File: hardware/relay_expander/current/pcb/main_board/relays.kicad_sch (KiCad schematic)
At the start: 82 parts, among them J10 Screw_Terminal_01x02, J11 Screw_Terminal_01x02, J4 Screw_Terminal_01x02, J5 Screw_Terminal_01x02, J6 Screw_Terminal_01x02, J7 Screw_Terminal_01x02, J8 Screw_Terminal_01x02, J9 Screw_Terminal_01x02, K1 SANYOU_SRD_Form_C, K2 SANYOU_SRD_Form_C, K3 SANYOU_SRD_Form_C, K4 SANYOU_SRD_Form_C, K5 SANYOU_SRD_Form_C, K6 SANYOU_SRD_Form_C, K7 SANYOU_SRD_Form_C, K8 SANYOU_SRD_Form_C, Q1 BC548, Q2 BC548, Q3 BC548, Q4 BC548, Q5 BC548, Q6 BC548, Q7 BC548, Q8 BC548, U2 TCMT4100, U3 TCMT4100

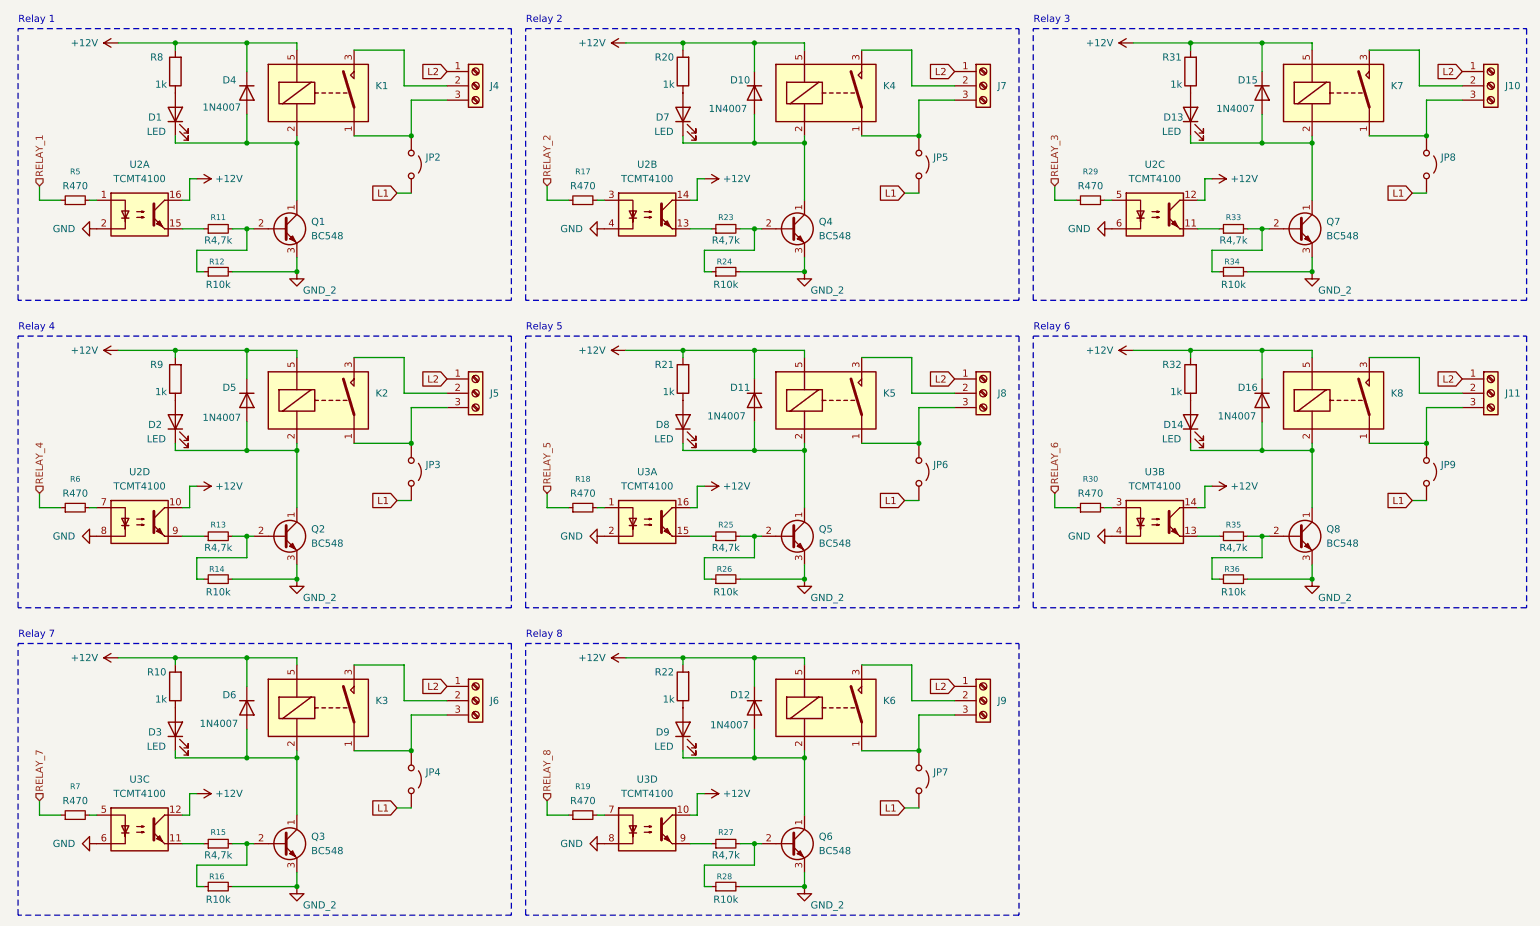
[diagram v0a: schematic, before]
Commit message: [ADD] ui board template
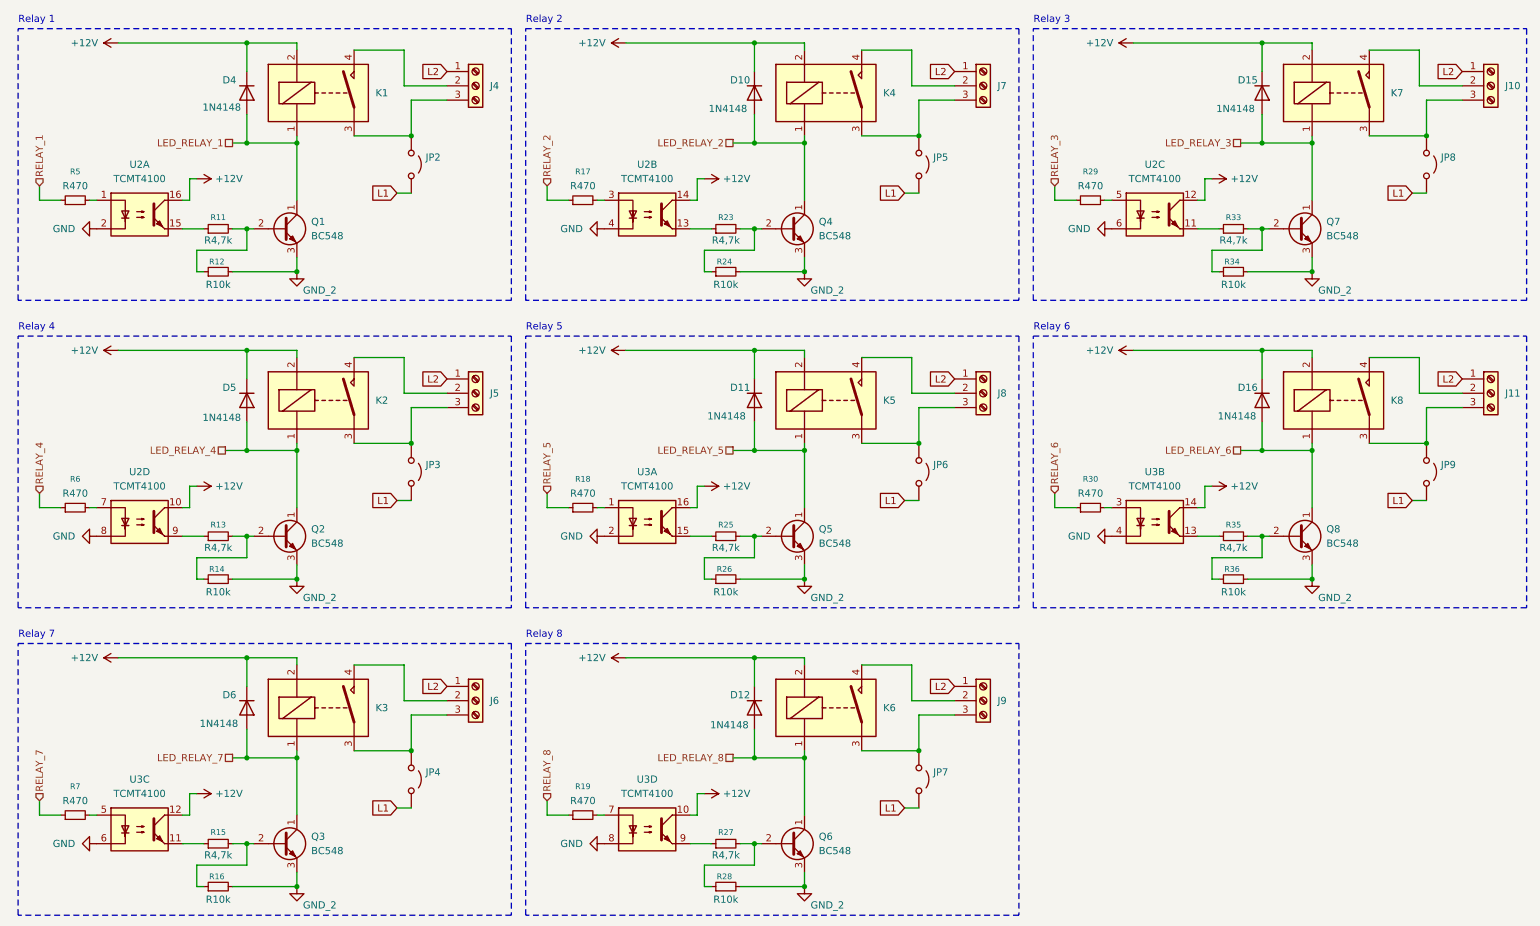
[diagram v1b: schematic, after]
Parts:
- removed D1, D13, D14, D2, D3, D7, D8, D9: LED, LED_SMD:LED_1206_3216Metric_Pad1.42x1.75mm_HandSolder, symbol Device:LED
- removed R10, R20, R21, R22, R31, R32, R8, R9: 1k, Resistor_SMD:R_1206_3216Metric_Pad1.30x1.75mm_HandSolder, symbol Device:R
- D10, D11, D12, D15, D16, D4, D5, D6: value 1N4007 -> 1N4148; footprint (none) -> Diode_SMD:D_SOD-123
- J10, J11, J5, J6, J7, J9: footprint Project_Parts_Footprints_Lib:TerminalBlock_Phoenix_MPT-0,5-3-2.54_1x03_P2.54mm_Horizontal -> footprints:Terminal_block_1x3_2,54
- J4: footprint Project_Parts_Footprints_Lib:TerminalBlock_Phoenix_MPT-0,5-3-2.54_1x03_P2.54mm_Horizontal -> TerminalBlock:TerminalBlock_Xinya_XY308-2.54-3P_1x03_P2.54mm_Horizontal
- J8: value Screw_Terminal_01x02 -> Screw_Terminal_01x03; footprint Project_Parts_Footprints_Lib:TerminalBlock_Phoenix_MPT-0,5-3-2.54_1x03_P2.54mm_Horizontal -> footprints:Terminal_block_1x3_2,54
- K1, K2, K3, K4, K5, K6, K7, K8: value SANYOU_SRD_Form_C -> HF46F-12-HS1; footprint templates_lib_footprints:Songle_SMI-SL-A -> homeautomation_core:relay_HF46F; symbol Relay:SANYOU_SRD_Form_A -> homeautomation_core:Relay_HF46F_Form_A
- R11, R12, R13, R14, R15, R16, R17, R18, R19, R23, R24, R25, R26, R27, R28, R29, R30, R33, R34, R35, R36, R5, R6, R7: footprint (none) -> Resistor_SMD:R_1206_3216Metric_Pad1.30x1.75mm_HandSolder
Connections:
- net +12V: now also K1.2, K2.2, K3.2, K4.2, K5.2, K6.2, K7.2, K8.2; no longer K1.5, K2.5, K3.5, K4.5, K5.5, K6.5, K7.5, K8.5
- net at J5.3 (Pin_3), JP3.1 (A): now also K2.3; no longer K2.1
- net LED_RELAY_6: now reaches D16.2 (A), Q8.1 (C)
- net LED_RELAY_6: now also K8.1; no longer K8.2
- net LED_RELAY_8: now reaches D12.2 (A), Q6.1 (C)
- net LED_RELAY_8: now also K6.1; no longer K6.2
- net LED_RELAY_4: now reaches D5.2 (A), Q2.1 (C)
- net LED_RELAY_4: now also K2.1; no longer K2.2
- net at J5.2 (Pin_2): now also K2.4; no longer K2.3
- net at J7.2 (Pin_2): now also K4.4; no longer K4.3
- net at J7.3 (Pin_3), JP5.1 (A): now also K4.3; no longer K4.1
- net at J11.3 (Pin_3), JP9.1 (A): now also K8.3; no longer K8.1
- net at J8.2 (Pin_2): now also K5.4; no longer K5.3
- net at J8.3 (Pin_3), JP6.1 (A): now also K5.3; no longer K5.1
- net LED_RELAY_5: now reaches D11.2 (A), Q5.1 (C)
- net LED_RELAY_5: now also K5.1; no longer K5.2
- net LED_RELAY_1: now reaches D4.2 (A), Q1.1 (C)
- net LED_RELAY_1: now also K1.1; no longer K1.2
- net LED_RELAY_7: now reaches D6.2 (A), Q3.1 (C)
- net LED_RELAY_7: now also K3.1; no longer K3.2
- net at J6.3 (Pin_3), JP4.1 (A): now also K3.3; no longer K3.1
- net at J6.2 (Pin_2): now also K3.4; no longer K3.3
- net at J10.2 (Pin_2): now also K7.4; no longer K7.3
- net at J10.3 (Pin_3), JP8.1 (A): now also K7.3; no longer K7.1
- net at J11.2 (Pin_2): now also K8.4; no longer K8.3
- net LED_RELAY_3: now reaches D15.2 (A), Q7.1 (C)
- net LED_RELAY_3: now also K7.1; no longer K7.2
- net LED_RELAY_2: now reaches D10.2 (A), Q4.1 (C)
- net LED_RELAY_2: now also K4.1; no longer K4.2
- net at J9.3 (Pin_3), JP7.1 (A): now also K6.3; no longer K6.1
- net at J9.2 (Pin_2): now also K6.4; no longer K6.3
- net at J4.2 (Pin_2): now also K1.4; no longer K1.3
- net at J4.3 (Pin_3), JP2.1 (A): now also K1.3; no longer K1.1

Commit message: [ADD] board connector
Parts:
- renumbered K4 to K2, K7 to K3, K2 to K4, K8 to K6, K3 to K7, K6 to K8, Q4 to Q2, Q7 to Q3, Q2 to Q4, Q8 to Q6, Q3 to Q7, Q6 to Q8
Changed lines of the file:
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@@
 		(dnp no)
 		(fields_autoplaced yes)
-		(property "Reference" "Q8"
+		(property "Reference" "Q6"
 			(at 247.65 106.6799 0)
 			(show_name no)
@@
 			(project "main_board"
 				(path "/14085887-8f36-46fe-a4da-c907d70eabd5/6a74995a-a263-4b43-94e4-c06372d97251"
-					(reference "Q8")
+					(reference "Q6")
 					(unit 1)
 				)
@@
 		(dnp no)
 		(fields_autoplaced yes)
-		(property "Reference" "Q6"
+		(property "Reference" "Q8"
 			(at 157.48 161.2899 0)
 			(show_name no)
@@
 			(project "main_board"
 				(path "/14085887-8f36-46fe-a4da-c907d70eabd5/6a74995a-a263-4b43-94e4-c06372d97251"
-					(reference "Q6")
+					(reference "Q8")
 					(unit 1)
 				)
@@
 		(dnp no)
 		(fields_autoplaced yes)
-		(property "Reference" "K2"
+		(property "Reference" "K4"
 			(at 78.74 83.8199 0)
 			(show_name no)
@@
 			(project "main_board"
 				(path "/14085887-8f36-46fe-a4da-c907d70eabd5/6a74995a-a263-4b43-94e4-c06372d97251"
-					(reference "K2")
+					(reference "K4")
 					(unit 1)
 				)
@@
 		(dnp no)
 		(fields_autoplaced yes)
-		(property "Reference" "Q2"
+		(property "Reference" "Q4"
 			(at 67.31 106.6799 0)
 			(show_name no)
@@
 			(project "main_board"
 				(path "/14085887-8f36-46fe-a4da-c907d70eabd5/6a74995a-a263-4b43-94e4-c06372d97251"
-					(reference "Q2")
+					(reference "Q4")
 					(unit 1)
 				)
@@
 		(dnp no)
 		(fields_autoplaced yes)
-		(property "Reference" "Q3"
+		(property "Reference" "Q7"
 			(at 67.31 161.2899 0)
 			(show_name no)
@@
 			(project "main_board"
 				(path "/14085887-8f36-46fe-a4da-c907d70eabd5/6a74995a-a263-4b43-94e4-c06372d97251"
-					(reference "Q3")
+					(reference "Q7")
 					(unit 1)
 				)
@@
 		(dnp no)
 		(fields_autoplaced yes)
-		(property "Reference" "K8"
+		(property "Reference" "K6"
 			(at 259.08 83.8199 0)
 			(show_name no)
@@
 			(project "main_board"
 				(path "/14085887-8f36-46fe-a4da-c907d70eabd5/6a74995a-a263-4b43-94e4-c06372d97251"
-					(reference "K8")
+					(reference "K6")
 					(unit 1)
 				)
@@
 		(dnp no)
 		(fields_autoplaced yes)
-		(property "Reference" "K7"
+		(property "Reference" "K3"
 			(at 259.08 29.2099 0)
 			(show_name no)
@@
 			(project "main_board"
 				(path "/14085887-8f36-46fe-a4da-c907d70eabd5/6a74995a-a263-4b43-94e4-c06372d97251"
-					(reference "K7")
+					(reference "K3")
 					(unit 1)
 				)
@@
 		(dnp no)
 		(fields_autoplaced yes)
-		(property "Reference" "K6"
+		(property "Reference" "K8"
 			(at 168.91 138.4299 0)
 			(show_name no)
@@
 			(project "main_board"
 				(path "/14085887-8f36-46fe-a4da-c907d70eabd5/6a74995a-a263-4b43-94e4-c06372d97251"
-					(reference "K6")
+					(reference "K8")
 					(unit 1)
 				)
@@
 		(dnp no)
 		(fields_autoplaced yes)
-		(property "Reference" "K3"
+		(property "Reference" "K7"
 			(at 78.74 138.4299 0)
 			(show_name no)
@@
 			(project "main_board"
 				(path "/14085887-8f36-46fe-a4da-c907d70eabd5/6a74995a-a263-4b43-94e4-c06372d97251"
-					(reference "K3")
+					(reference "K7")
 					(unit 1)
 				)
@@
 		(dnp no)
 		(fields_autoplaced yes)
-		(property "Reference" "K4"
+		(property "Reference" "K2"
 			(at 168.91 29.2099 0)
 			(show_name no)
@@
 			(project "main_board"
 				(path "/14085887-8f36-46fe-a4da-c907d70eabd5/6a74995a-a263-4b43-94e4-c06372d97251"
-					(reference "K4")
+					(reference "K2")
 					(unit 1)
 				)
@@
 		(dnp no)
 		(fields_autoplaced yes)
-		(property "Reference" "Q4"
+		(property "Reference" "Q2"
 			(at 157.48 52.0699 0)
 			(show_name no)
@@
 			(project "main_board"
 				(path "/14085887-8f36-46fe-a4da-c907d70eabd5/6a74995a-a263-4b43-94e4-c06372d97251"
-					(reference "Q4")
+					(reference "Q2")
 					(unit 1)
 				)
@@
 		(dnp no)
 		(fields_autoplaced yes)
-		(property "Reference" "Q7"
+		(property "Reference" "Q3"
 			(at 247.65 52.0699 0)
 			(show_name no)
@@
 			(project "main_board"
 				(path "/14085887-8f36-46fe-a4da-c907d70eabd5/6a74995a-a263-4b43-94e4-c06372d97251"
-					(reference "Q7")
+					(reference "Q3")
 					(unit 1)
 				)

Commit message: [ADD] routing on main pcb board
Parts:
- J10, J11, J5, J6, J7, J8, J9: footprint footprints:Terminal_block_1x3_2,54 -> homeautomation_core:TerminalBlock_Phoenix_MPT-0,5-3-2.54_1x03_P2.54mm_Horizontal_RELAY
- J4: footprint TerminalBlock:TerminalBlock_Xinya_XY308-2.54-3P_1x03_P2.54mm_Horizontal -> homeautomation_core:TerminalBlock_Phoenix_MPT-0,5-3-2.54_1x03_P2.54mm_Horizontal_RELAY
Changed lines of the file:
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@@
 			)
 		)
-		(property "Footprint" "footprints:Terminal_block_1x3_2,54"
+		(property "Footprint" "homeautomation_core:TerminalBlock_Phoenix_MPT-0,5-3-2.54_1x03_P2.54mm_Horizontal_RELAY"
 			(at 186.69 27.94 0)
 			(hide yes)
@@
 			)
 		)
-		(property "Footprint" "footprints:Terminal_block_1x3_2,54"
+		(property "Footprint" "homeautomation_core:TerminalBlock_Phoenix_MPT-0,5-3-2.54_1x03_P2.54mm_Horizontal_RELAY"
 			(at 186.69 82.55 0)
 			(hide yes)
@@
 			)
 		)
-		(property "Footprint" "footprints:Terminal_block_1x3_2,54"
+		(property "Footprint" "homeautomation_core:TerminalBlock_Phoenix_MPT-0,5-3-2.54_1x03_P2.54mm_Horizontal_RELAY"
 			(at 96.52 137.16 0)
 			(hide yes)
@@
 			)
 		)
-		(property "Footprint" "footprints:Terminal_block_1x3_2,54"
+		(property "Footprint" "homeautomation_core:TerminalBlock_Phoenix_MPT-0,5-3-2.54_1x03_P2.54mm_Horizontal_RELAY"
 			(at 276.86 27.94 0)
 			(hide yes)
@@
 			)
 		)
-		(property "Footprint" "footprints:Terminal_block_1x3_2,54"
+		(property "Footprint" "homeautomation_core:TerminalBlock_Phoenix_MPT-0,5-3-2.54_1x03_P2.54mm_Horizontal_RELAY"
 			(at 96.52 82.55 0)
 			(hide yes)
@@
 			)
 		)
-		(property "Footprint" "TerminalBlock:TerminalBlock_Xinya_XY308-2.54-3P_1x03_P2.54mm_Horizontal"
+		(property "Footprint" "homeautomation_core:TerminalBlock_Phoenix_MPT-0,5-3-2.54_1x03_P2.54mm_Horizontal_RELAY"
 			(at 96.52 27.94 0)
 			(hide yes)
@@
 			)
 		)
-		(property "Footprint" "footprints:Terminal_block_1x3_2,54"
+		(property "Footprint" "homeautomation_core:TerminalBlock_Phoenix_MPT-0,5-3-2.54_1x03_P2.54mm_Horizontal_RELAY"
 			(at 276.86 82.55 0)
 			(hide yes)
@@
 			)
 		)
-		(property "Footprint" "footprints:Terminal_block_1x3_2,54"
+		(property "Footprint" "homeautomation_core:TerminalBlock_Phoenix_MPT-0,5-3-2.54_1x03_P2.54mm_Horizontal_RELAY"
 			(at 186.69 137.16 0)
 			(hide yes)

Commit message: [FIX] add 12V trace for expanders and generate gerber for all relays related boards
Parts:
- J10, J11, J4, J5, J6, J7, J9: value Screw_Terminal_01x02 -> Screw_Terminal_01x03
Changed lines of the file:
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@@
 			)
 		)
-		(property "Value" "Screw_Terminal_01x02"
+		(property "Value" "Screw_Terminal_01x03"
 			(at 189.23 30.4799 0)
 			(hide yes)
@@
 			)
 		)
-		(property "Value" "Screw_Terminal_01x02"
+		(property "Value" "Screw_Terminal_01x03"
 			(at 99.06 139.6999 0)
 			(hide yes)
@@
 			)
 		)
-		(property "Value" "Screw_Terminal_01x02"
+		(property "Value" "Screw_Terminal_01x03"
 			(at 279.4 30.4799 0)
 			(hide yes)
@@
 			)
 		)
-		(property "Value" "Screw_Terminal_01x02"
+		(property "Value" "Screw_Terminal_01x03"
 			(at 99.06 85.0899 0)
 			(hide yes)
@@
 			)
 		)
-		(property "Value" "Screw_Terminal_01x02"
+		(property "Value" "Screw_Terminal_01x03"
 			(at 99.06 30.4799 0)
 			(hide yes)
@@
 			)
 		)
-		(property "Value" "Screw_Terminal_01x02"
+		(property "Value" "Screw_Terminal_01x03"
 			(at 279.4 85.0899 0)
 			(hide yes)
@@
 			)
 		)
-		(property "Value" "Screw_Terminal_01x02"
+		(property "Value" "Screw_Terminal_01x03"
 			(at 189.23 139.6999 0)
 			(hide yes)
